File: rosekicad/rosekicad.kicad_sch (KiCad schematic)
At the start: 74 parts, among them J1 Solenoid, J10 Solenoid, J11 Solenoid, J12 Solenoid, J13 UV Lights, J14 LED Lights, J15 DMX Cable, J16 Barrel_Jack_MountingPin, J2 Solenoid, J3 Solenoid, J4 Solenoid, J5 Solenoid, J6 Solenoid, J7 Solenoid, J8 Solenoid, J9 Solenoid, Q1 2N2222, Q10 2N2222, Q11 2N2222, Q12 2N2222, Q13 2N2222, Q14 2N2222, Q15 2N2222, Q2 2N2222, Q3 2N2222, Q4 2N2222, Q5 2N2222, Q6 2N2222, Q7 2N2222, Q8 2N2222, Q9 2N2222, U1 MAX485E

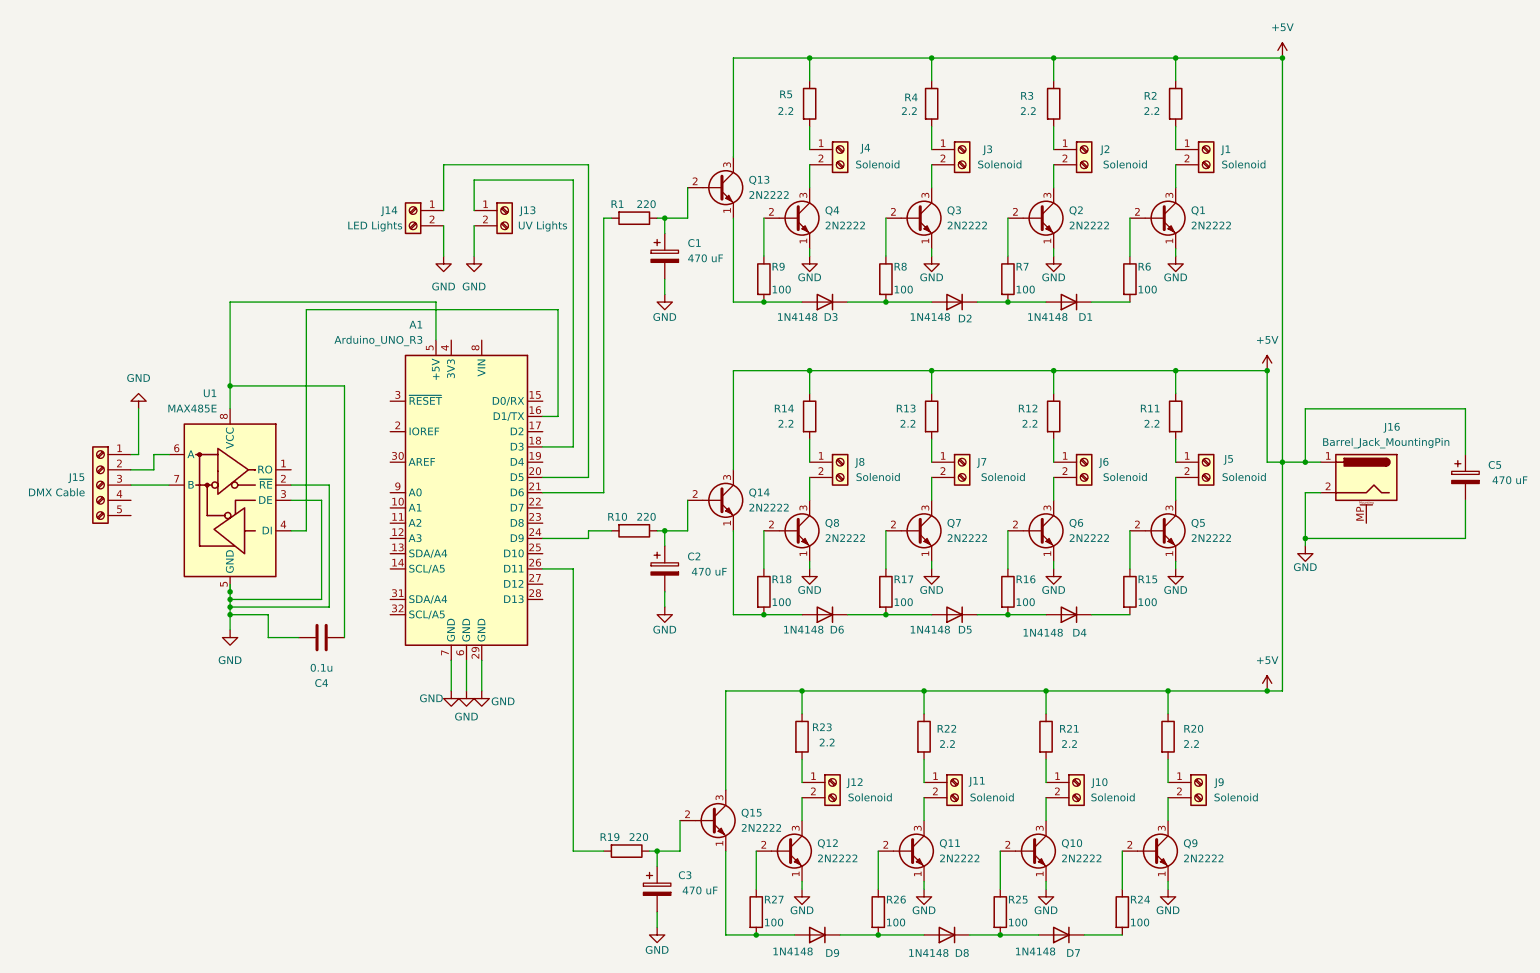
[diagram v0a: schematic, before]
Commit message: mounting holes
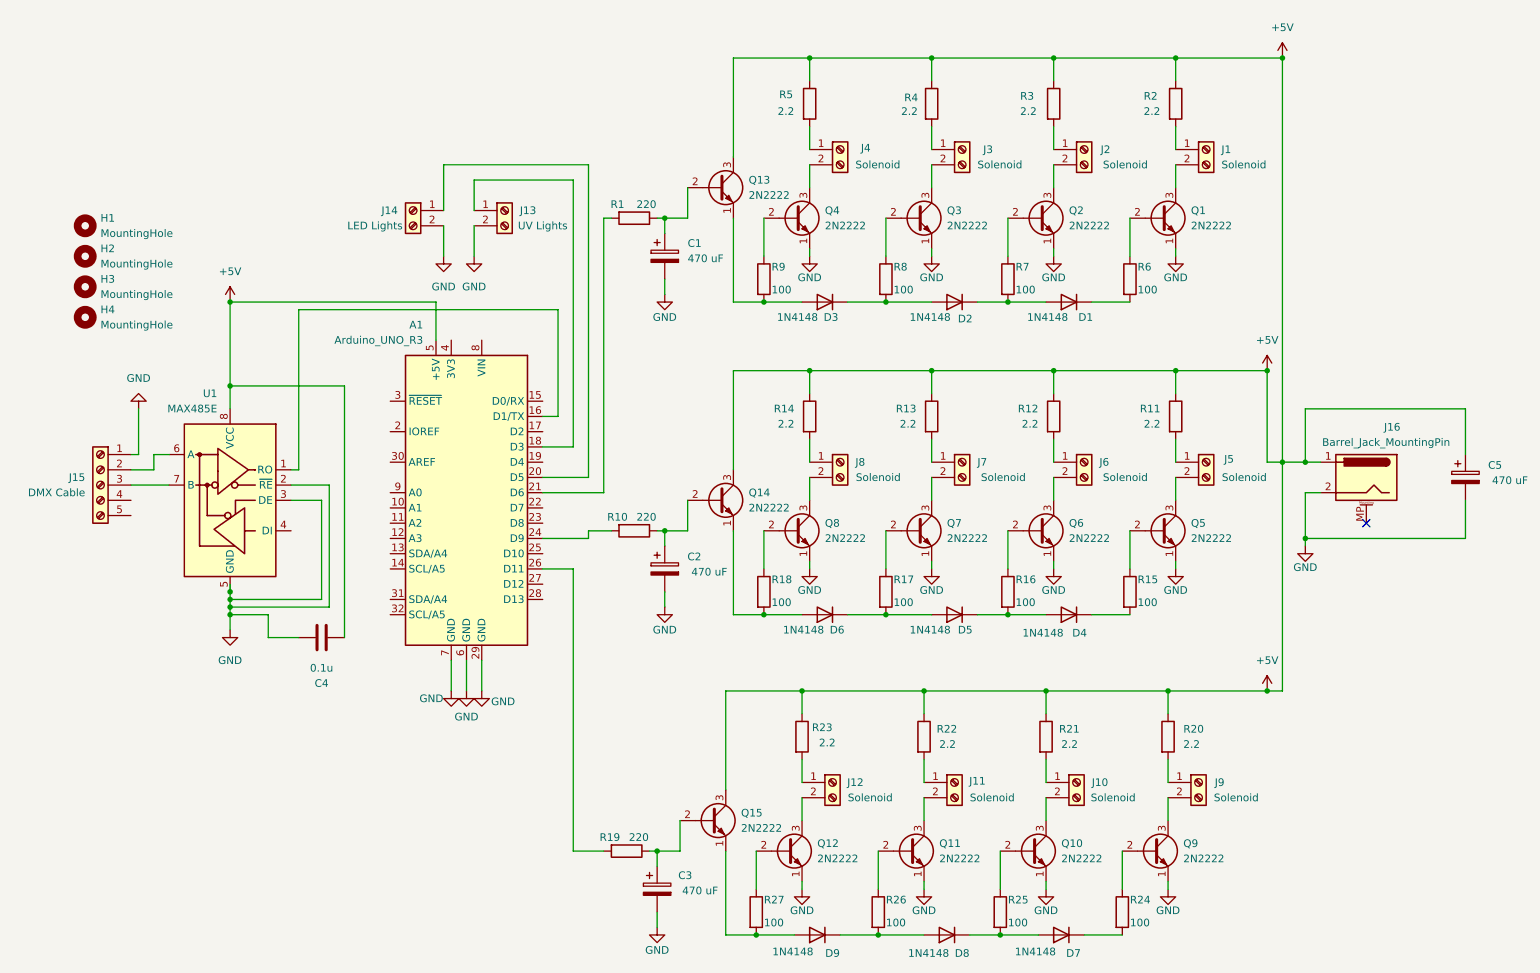
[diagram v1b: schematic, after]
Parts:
- added H1, H2, H3, H4: MountingHole, MountingHole:MountingHole_4.5mm_Pad, symbol Mechanical:MountingHole
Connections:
- net +5V: now also A1.5 (+5V), C4.1, U1.8 (VCC)
- net at A1.16 (D1/TX): now also U1.1 (RO); no longer U1.4 (DI)
- no-connect marks 0 -> 1

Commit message: finalized pcb main
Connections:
- net at A1.15 (D0/RX): now also U1.1 (RO)
- net at A1.16 (D1/TX): no longer U1.1 (RO)
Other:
- moved on the sheet: C4, J15
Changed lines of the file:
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@@
 	)
 	(junction
-		(at 49.53 74.93)
-		(diameter 0)
-		(color 0 0 0 0)
-	)
-	(junction
 		(at 186.69 72.39)
 		(diameter 0)
@@
 	)
 	(junction
+		(at 49.53 113.03)
+		(diameter 0)
+		(color 0 0 0 0)
+	)
+	(junction
 		(at 158.75 113.03)
 		(diameter 0)
@@
 	)
 	(junction
-		(at 49.53 113.03)
-		(diameter 0)
-		(color 0 0 0 0)
-	)
-	(junction
 		(at 146.05 20.32)
 		(diameter 0)
@@
 	(wire
 		(pts
-			(xy 60.96 116.84) (xy 55.88 116.84)
-		)
-		(stroke
-			(width 0)
-			(type default)
-		)
-	)
-	(wire
-		(pts
-			(xy 104.14 62.23) (xy 104.14 80.01)
+			(xy 104.14 62.23) (xy 104.14 77.47)
 		)
 		(stroke
@@
 	(wire
 		(pts
-			(xy 207.01 52.07) (xy 207.01 53.34)
+			(xy 33.02 102.87) (xy 33.02 105.41)
 		)
 		(stroke
@@
 	(wire
 		(pts
-			(xy 133.35 72.39) (xy 133.35 88.9)
+			(xy 207.01 52.07) (xy 207.01 53.34)
 		)
 		(stroke
@@
 	(wire
 		(pts
-			(xy 133.35 99.06) (xy 133.35 113.03)
+			(xy 133.35 72.39) (xy 133.35 88.9)
 		)
 		(stroke
@@
 	(wire
 		(pts
-			(xy 166.37 31.75) (xy 166.37 35.56)
+			(xy 133.35 99.06) (xy 133.35 113.03)
 		)
 		(stroke
@@
 	(wire
 		(pts
-			(xy 205.74 137.16) (xy 205.74 140.97)
+			(xy 166.37 31.75) (xy 166.37 35.56)
 		)
 		(stroke
@@
 	(wire
 		(pts
-			(xy 166.37 38.1) (xy 166.37 41.91)
+			(xy 205.74 137.16) (xy 205.74 140.97)
 		)
 		(stroke
@@
 	(wire
 		(pts
-			(xy 49.53 115.57) (xy 49.53 113.03)
+			(xy 166.37 38.1) (xy 166.37 41.91)
 		)
 		(stroke
@@
 	(wire
 		(pts
-			(xy 68.58 74.93) (xy 68.58 116.84)
-		)
-		(stroke
-			(width 0)
-			(type default)
-		)
-	)
-	(wire
-		(pts
 			(xy 121.92 109.22) (xy 121.92 111.76)
 		)
@@
 	(wire
 		(pts
+			(xy 36.83 91.44) (xy 39.37 91.44)
+		)
+		(stroke
+			(width 0)
+			(type default)
+		)
+	)
+	(wire
+		(pts
 			(xy 90.17 40.64) (xy 90.17 45.72)
 		)
@@
 	(wire
 		(pts
-			(xy 33.02 91.44) (xy 39.37 91.44)
+			(xy 49.53 113.03) (xy 49.53 115.57)
+		)
+		(stroke
+			(width 0)
+			(type default)
+		)
+	)
+	(wire
+		(pts
+			(xy 33.02 88.9) (xy 36.83 88.9)
 		)
 		(stroke
@@
 	(wire
 		(pts
+			(xy 33.02 113.03) (xy 49.53 113.03)
+		)
+		(stroke
+			(width 0)
+			(type default)
+		)
+	)
+	(wire
+		(pts
 			(xy 146.05 72.39) (xy 166.37 72.39)
 		)
@@
 	(wire
 		(pts
-			(xy 39.37 86.36) (xy 36.83 86.36)
-		)
-		(stroke
-			(width 0)
-			(type default)
-		)
-	)
-	(wire
-		(pts
 			(xy 125.73 41.91) (xy 125.73 46.99)
 		)
@@
 	(wire
 		(pts
-			(xy 49.53 78.74) (xy 49.53 74.93)
+			(xy 49.53 60.96) (xy 49.53 78.74)
 		)
 		(stroke
@@
 	(wire
 		(pts
-			(xy 36.83 88.9) (xy 33.02 88.9)
+			(xy 33.02 86.36) (xy 39.37 86.36)
 		)
 		(stroke
@@
 	(wire
 		(pts
-			(xy 36.83 86.36) (xy 36.83 88.9)
-		)
-		(stroke
-			(width 0)
-			(type default)
-		)
-	)
-	(wire
-		(pts
 			(xy 101.6 90.17) (xy 109.22 90.17)
 		)
@@
 	(wire
 		(pts
-			(xy 49.53 74.93) (xy 49.53 60.96)
-		)
-		(stroke
-			(width 0)
-			(type default)
-		)
-	)
-	(wire
-		(pts
 			(xy 224.79 125.73) (xy 222.25 125.73)
 		)
@@
 	(wire
 		(pts
+			(xy 36.83 88.9) (xy 36.83 91.44)
+		)
+		(stroke
+			(width 0)
+			(type default)
+		)
+	)
+	(wire
+		(pts
 			(xy 207.01 90.17) (xy 207.01 93.98)
 		)
@@
 	(wire
 		(pts
-			(xy 34.29 86.36) (xy 33.02 86.36)
+			(xy 34.29 83.82) (xy 33.02 83.82)
 		)
 		(stroke
@@
 	(wire
 		(pts
-			(xy 138.43 60.96) (xy 144.78 60.96)
+			(xy 104.14 77.47) (xy 101.6 77.47)
 		)
 		(stroke
@@
 	(wire
 		(pts
-			(xy 166.37 20.32) (xy 166.37 24.13)
+			(xy 138.43 60.96) (xy 144.78 60.96)
 		)
 		(stroke
@@
 	(wire
 		(pts
-			(xy 186.69 72.39) (xy 207.01 72.39)
+			(xy 166.37 20.32) (xy 166.37 24.13)
 		)
 		(stroke
@@
 	(wire
 		(pts
-			(xy 151.13 166.37) (xy 157.48 166.37)
+			(xy 186.69 72.39) (xy 207.01 72.39)
 		)
 		(stroke
@@
 	(wire
 		(pts
-			(xy 104.14 80.01) (xy 101.6 80.01)
+			(xy 151.13 166.37) (xy 157.48 166.37)
 		)
 		(stroke
@@
 	(wire
 		(pts
-			(xy 55.88 113.03) (xy 49.53 113.03)
-		)
-		(stroke
-			(width 0)
-			(type default)
-		)
-	)
-	(wire
-		(pts
 			(xy 109.22 90.17) (xy 109.22 38.1)
 		)
@@
 	(wire
 		(pts
-			(xy 34.29 78.74) (xy 34.29 86.36)
+			(xy 34.29 78.74) (xy 34.29 83.82)
 		)
 		(stroke
@@
 	(wire
 		(pts
-			(xy 49.53 74.93) (xy 68.58 74.93)
-		)
-		(stroke
-			(width 0)
-			(type default)
-		)
-	)
-	(wire
-		(pts
 			(xy 179.07 99.06) (xy 179.07 105.41)
 		)
@@
 	(wire
 		(pts
-			(xy 55.88 116.84) (xy 55.88 113.03)
-		)
-		(stroke
-			(width 0)
-			(type default)
-		)
-	)
-	(wire
-		(pts
 			(xy 124.46 152.4) (xy 120.65 152.4)
 		)
@@
 	)
 	(symbol
+		(lib_id "power:+5V")
+		(at 33.02 102.87 0)
+		(unit 1)
+		(exclude_from_sim no)
+		(in_bom yes)
+		(on_board yes)
+		(dnp no)
+		(fields_autoplaced yes)
+		(property "Reference" "#PWR014"
+			(at 33.02 106.68 0)
+			(effects
+				(font
+					(size 1.27 1.27)
+				)
+				(hide yes)
+			)
+		)
+		(property "Value" "+5V"
+			(at 33.02 97.79 0)
+			(effects
+				(font
+					(size 1.27 1.27)
+				)
+			)
+		)
+		(property "Footprint" ""
+			(at 33.02 102.87 0)
+			(effects
+				(font
+					(size 1.27 1.27)
+				)
+				(hide yes)
+			)
+		)
+		(property "Datasheet" ""
+			(at 33.02 102.87 0)
+			(effects
+				(font
+					(size 1.27 1.27)
+				)
+				(hide yes)
+			)
+		)
+		(property "Description" "Power symbol creates a global label with name \"+5V\""
+			(at 33.02 102.87 0)
+			(effects
+				(font
+					(size 1.27 1.27)
+				)
+				(hide yes)
+			)
+		)
+		(pin "1"
+		)
+		(instances
+			(project ""
+				(path "/0657b7e7-94cf-4389-b691-da93263aa22a"
+					(reference "#PWR014")
+					(unit 1)
+				)
+			)
+		)
+	)
+	(symbol
 		(lib_id "MCU_Module:Arduino_UNO_R3")
 		(at 88.9 92.71 0)
@@
 	(symbol
 		(lib_id "Connector:Screw_Terminal_01x05")
-		(at 27.94 91.44 0)
+		(at 27.94 88.9 0)
 		(mirror y)
 		(unit 1)
@@
 		(fields_autoplaced yes)
 		(property "Reference" "J15"
-			(at 25.4 90.1699 0)
+			(at 25.4 87.6299 0)
 			(effects
 				(font
@@
 		)
 		(property "Value" "DMX Cable"
-			(at 25.4 92.7099 0)
+			(at 25.4 90.1699 0)
 			(effects
 				(font
@@
 		)
 		(property "Footprint" "TerminalBlock:TerminalBlock_MaiXu_MX126-5.0-05P_1x05_P5.00mm"
-			(at 27.94 91.44 0)
+			(at 27.94 88.9 0)
 			(effects
 				(font
@@
 		)
 		(property "Datasheet" "~"
-			(at 27.94 91.44 0)
+			(at 27.94 88.9 0)
 			(effects
 				(font
@@
 		)
 		(property "Description" "Generic screw terminal, single row, 01x05, script generated (kicad-library-utils/schlib/autogen/connector/)"
-			(at 27.94 91.44 0)
+			(at 27.94 88.9 0)
 			(effects
 				(font
@@
 	(symbol
 		(lib_id "Device:C")
-		(at 64.77 116.84 270)
+		(at 33.02 109.22 0)
 		(unit 1)
 		(exclude_from_sim no)
@@
 		(dnp no)
 		(property "Reference" "C4"
-			(at 64.77 124.46 90)
+			(at 37.338 107.95 0)
 			(effects
 				(font
@@
 		)
 		(property "Value" "0.1u"
-			(at 64.77 121.92 90)
+			(at 37.846 110.49 0)
 			(effects
 				(font
@@
 		)
 		(property "Footprint" "Capacitor_THT:CP_Radial_D5.0mm_P2.00mm"
-			(at 60.96 117.8052 0)
+			(at 33.9852 113.03 0)
 			(effects
 				(font
@@
 		)
 		(property "Datasheet" "~"
-			(at 64.77 116.84 0)
+			(at 33.02 109.22 0)
 			(effects
 				(font
@@
 		)
 		(property "Description" "Unpolarized capacitor"
-			(at 64.77 116.84 0)
+			(at 33.02 109.22 0)
 			(effects
 				(font

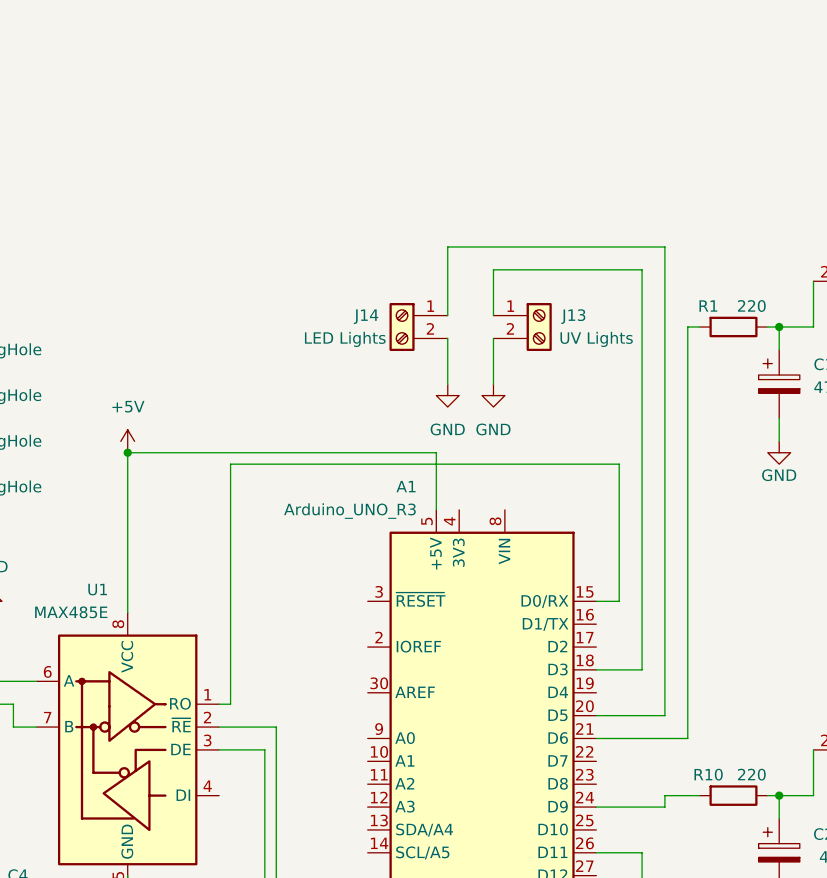
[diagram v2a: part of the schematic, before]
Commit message: mosfets added
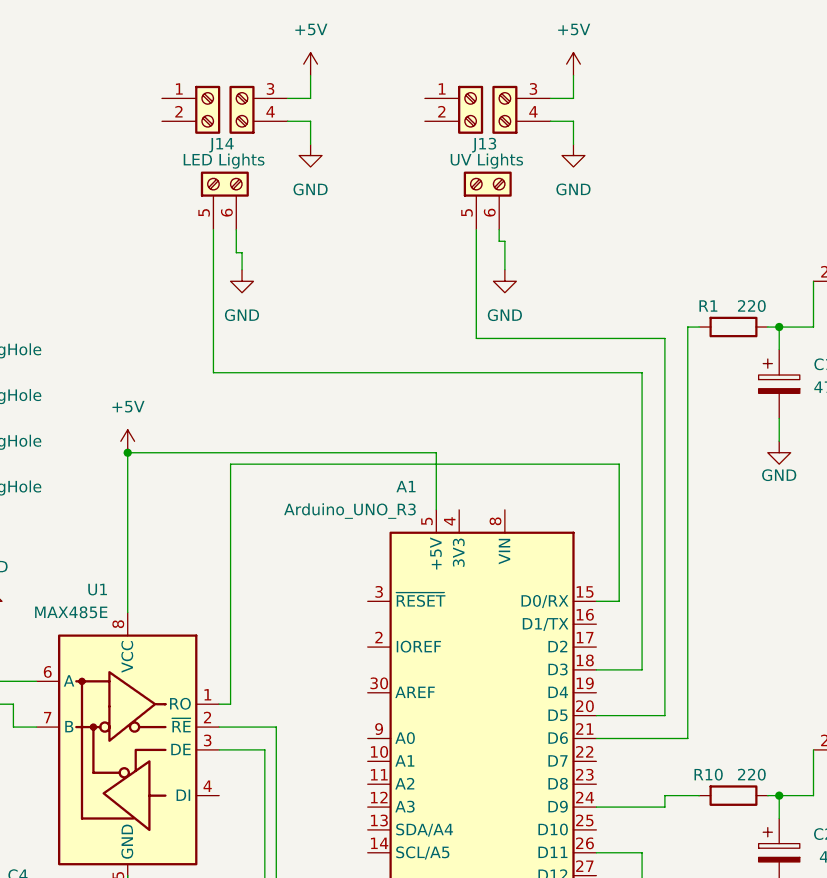
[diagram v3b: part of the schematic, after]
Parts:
- J13, J14: footprint TerminalBlock:TerminalBlock_MaiXu_MX126-5.0-02P_1x02_P5.00mm -> rosekicad:MOSFET Switch Driver Module
- Q1, Q10, Q11, Q12, Q13, Q14, Q15, Q2, Q3, Q4, Q5, Q6, Q7, Q8, Q9: footprint Package_TO_SOT_THT:TO-92_Inline -> Package_TO_SOT_THT:TO-92_Inline_Wide
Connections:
- net +5V: now also J13.3 (VIN+), J14.3 (VIN+)
- net GND: now also J13.4 (VIN-), J13.6 (GND), J14.4 (VIN-), J14.6 (GND); no longer J13.2 (Pin_2), J14.2 (Pin_2)
- net at A1.20 (D5): now also J13.5 (trig); no longer J14.1 (Pin_1)
- net at A1.18 (D3): now also J14.5 (trig); no longer J13.1 (Pin_1)

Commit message: final
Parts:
- removed J13: UV Lights, rosekicad:MOSFET Switch Driver Module, symbol Connector:Screw_Terminal_01x02
- removed J14: LED Lights, rosekicad:MOSFET Switch Driver Module, symbol Connector:Screw_Terminal_01x02
- added U2, U3: MOSFET_module, rosekicad:MOSFET Switch Driver Module, symbol MOSFET_module:MOSFET_module
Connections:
- net +5V: now also U2.3 (VIN+), U3.3 (VIN+)
- net GND: now also U2.4 (VIN-), U2.6 (GND), U3.4 (VIN-), U3.6 (GND)
- net at A1.18 (D3): now also U2.5 (PWM)
- net at A1.20 (D5): now also U3.5 (PWM)
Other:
- moved on the sheet: H1, H2, H3, H4

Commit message: final
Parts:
- R11, R12, R13, R14, R2, R20, R21, R22, R23, R3, R4, R5: footprint Resistor_THT:R_Axial_DIN0207_L6.3mm_D2.5mm_P7.62mm_Horizontal -> Resistor_THT:R_Axial_DIN0414_L11.9mm_D4.5mm_P15.24mm_Horizontal
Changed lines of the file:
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@@
 			)
 		)
-		(property "Footprint" "Resistor_THT:R_Axial_DIN0207_L6.3mm_D2.5mm_P7.62mm_Horizontal"
+		(property "Footprint" "Resistor_THT:R_Axial_DIN0414_L11.9mm_D4.5mm_P15.24mm_Horizontal"
 			(at 143.002 133.35 90)
 			(effects
@@
 			)
 		)
-		(property "Footprint" "Resistor_THT:R_Axial_DIN0207_L6.3mm_D2.5mm_P7.62mm_Horizontal"
+		(property "Footprint" "Resistor_THT:R_Axial_DIN0414_L11.9mm_D4.5mm_P15.24mm_Horizontal"
 			(at 184.912 80.01 90)
 			(effects
@@
 			)
 		)
-		(property "Footprint" "Resistor_THT:R_Axial_DIN0207_L6.3mm_D2.5mm_P7.62mm_Horizontal"
+		(property "Footprint" "Resistor_THT:R_Axial_DIN0414_L11.9mm_D4.5mm_P15.24mm_Horizontal"
 			(at 144.272 80.01 90)
 			(effects
@@
 			)
 		)
-		(property "Footprint" "Resistor_THT:R_Axial_DIN0207_L6.3mm_D2.5mm_P7.62mm_Horizontal"
+		(property "Footprint" "Resistor_THT:R_Axial_DIN0414_L11.9mm_D4.5mm_P15.24mm_Horizontal"
 			(at 205.232 27.94 90)
 			(effects
@@
 			)
 		)
-		(property "Footprint" "Resistor_THT:R_Axial_DIN0207_L6.3mm_D2.5mm_P7.62mm_Horizontal"
+		(property "Footprint" "Resistor_THT:R_Axial_DIN0414_L11.9mm_D4.5mm_P15.24mm_Horizontal"
 			(at 164.592 80.01 90)
 			(effects
@@
 			)
 		)
-		(property "Footprint" "Resistor_THT:R_Axial_DIN0207_L6.3mm_D2.5mm_P7.62mm_Horizontal"
+		(property "Footprint" "Resistor_THT:R_Axial_DIN0414_L11.9mm_D4.5mm_P15.24mm_Horizontal"
 			(at 203.962 133.35 90)
 			(effects
@@
 			)
 		)
-		(property "Footprint" "Resistor_THT:R_Axial_DIN0207_L6.3mm_D2.5mm_P7.62mm_Horizontal"
+		(property "Footprint" "Resistor_THT:R_Axial_DIN0414_L11.9mm_D4.5mm_P15.24mm_Horizontal"
 			(at 183.642 133.35 90)
 			(effects
@@
 			)
 		)
-		(property "Footprint" "Resistor_THT:R_Axial_DIN0207_L6.3mm_D2.5mm_P7.62mm_Horizontal"
+		(property "Footprint" "Resistor_THT:R_Axial_DIN0414_L11.9mm_D4.5mm_P15.24mm_Horizontal"
 			(at 205.232 80.01 90)
 			(effects
@@
 			)
 		)
-		(property "Footprint" "Resistor_THT:R_Axial_DIN0207_L6.3mm_D2.5mm_P7.62mm_Horizontal"
+		(property "Footprint" "Resistor_THT:R_Axial_DIN0414_L11.9mm_D4.5mm_P15.24mm_Horizontal"
 			(at 163.322 133.35 90)
 			(effects
@@
 			)
 		)
-		(property "Footprint" "Resistor_THT:R_Axial_DIN0207_L6.3mm_D2.5mm_P7.62mm_Horizontal"
+		(property "Footprint" "Resistor_THT:R_Axial_DIN0414_L11.9mm_D4.5mm_P15.24mm_Horizontal"
 			(at 144.272 27.94 90)
 			(effects
@@
 			)
 		)
-		(property "Footprint" "Resistor_THT:R_Axial_DIN0207_L6.3mm_D2.5mm_P7.62mm_Horizontal"
+		(property "Footprint" "Resistor_THT:R_Axial_DIN0414_L11.9mm_D4.5mm_P15.24mm_Horizontal"
 			(at 164.592 27.94 90)
 			(effects
@@
 			)
 		)
-		(property "Footprint" "Resistor_THT:R_Axial_DIN0207_L6.3mm_D2.5mm_P7.62mm_Horizontal"
+		(property "Footprint" "Resistor_THT:R_Axial_DIN0414_L11.9mm_D4.5mm_P15.24mm_Horizontal"
 			(at 184.912 27.94 90)
 			(effects
